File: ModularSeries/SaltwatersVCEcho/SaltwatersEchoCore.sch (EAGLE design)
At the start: 109 parts, among them IC1 PT2399DIL16, Q1 2N3906, Q2 2N3906, Q3 2N3906, Q4 2N3906, Q5 2N3904, Q6 2N3904

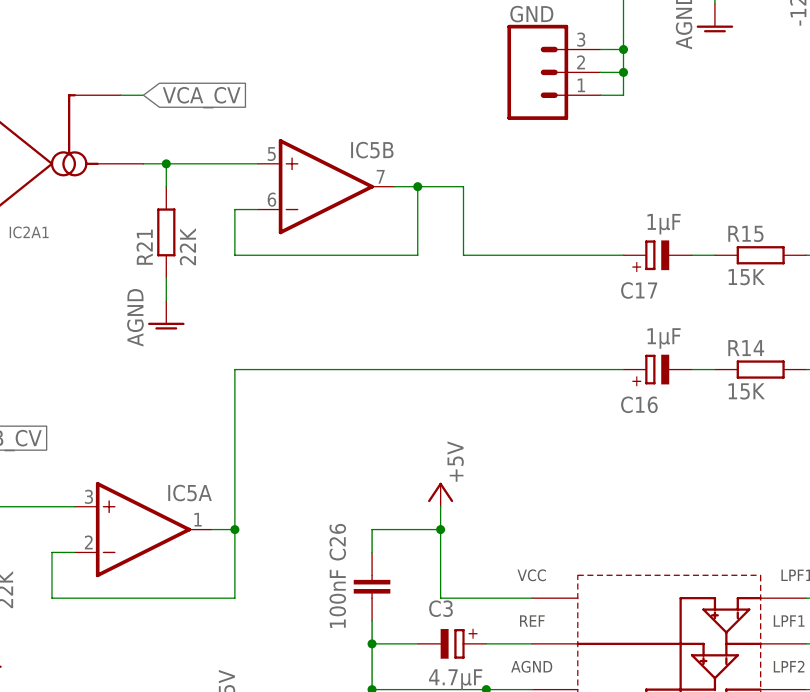
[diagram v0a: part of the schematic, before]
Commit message: All active BOMs updated to new header standard
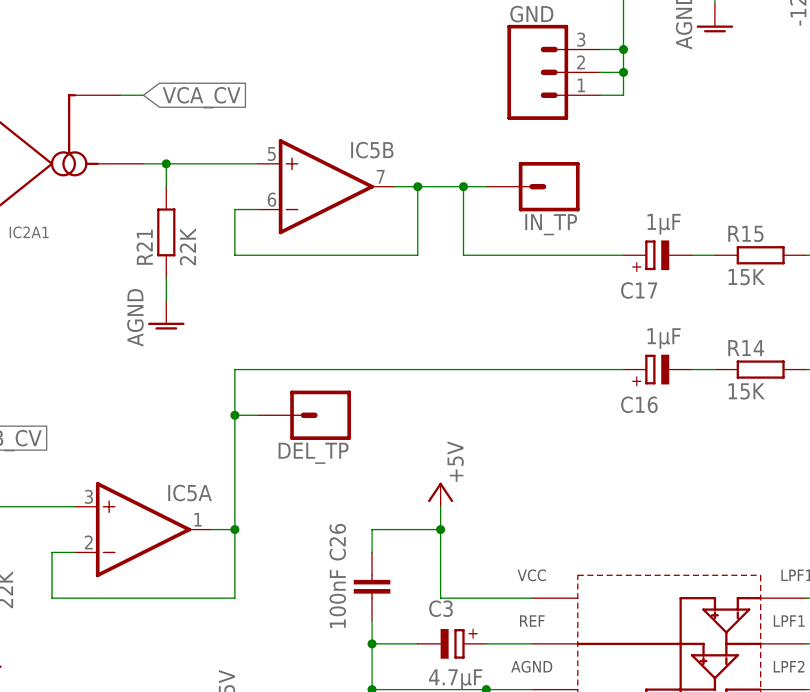
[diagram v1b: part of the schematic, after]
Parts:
- added DEL_TP, IN_TP: 1XWIREPAD, ElectricNoodleBox:1XWIREPAD
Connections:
- net FB_RTN: now also DEL_TP.1
- net N$34: now also IN_TP.1
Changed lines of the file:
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@@
 <part name="AGND21" library="supply1" library_urn="urn:adsk.eagle:library:371" deviceset="AGND" device=""/>
 <part name="GND" library="ElectricNoodleBox" deviceset="3XWIREPAD" device=""/>
+<part name="IN_TP" library="ElectricNoodleBox" deviceset="1XWIREPAD" device=""/>
+<part name="DEL_TP" library="ElectricNoodleBox" deviceset="1XWIREPAD" device=""/>
 </parts>
 <sheets>
@@
 <instance part="GND" gate="G$1" x="55.88" y="127" smashed="yes">
 <attribute name="NAME" x="53.34" y="132.588" size="1.778" layer="95" font="vector"/>
+</instance>
+<instance part="IN_TP" gate="G$1" x="58.42" y="114.3" smashed="yes" rot="R180">
+<attribute name="NAME" x="60.96" y="111.252" size="1.778" layer="95" font="vector" rot="R180"/>
+</instance>
+<instance part="DEL_TP" gate="G$1" x="33.02" y="88.9" smashed="yes" rot="R180">
+<attribute name="NAME" x="35.56" y="85.852" size="1.778" layer="95" font="vector" rot="R180"/>
 </instance>
 </instances>
@@
 <wire x1="22.86" y1="76.2" x2="20.32" y2="76.2" width="0.1524" layer="91"/>
 <junction x="22.86" y="76.2"/>
-<wire x1="22.86" y1="76.2" x2="22.86" y2="93.98" width="0.1524" layer="91"/>
+<wire x1="22.86" y1="76.2" x2="22.86" y2="88.9" width="0.1524" layer="91"/>
+<pinref part="DEL_TP" gate="G$1" pin="1"/>
+<wire x1="22.86" y1="88.9" x2="22.86" y2="93.98" width="0.1524" layer="91"/>
+<wire x1="22.86" y1="88.9" x2="25.4" y2="88.9" width="0.1524" layer="91"/>
+<junction x="22.86" y="88.9"/>
 </segment>
 </net>
@@
 <pinref part="C17" gate="G$1" pin="+"/>
 <wire x1="66.04" y1="106.68" x2="48.26" y2="106.68" width="0.1524" layer="91"/>
-</segment>
-</net>
+<pinref part="IN_TP" gate="G$1" pin="1"/>
+<wire x1="48.26" y1="114.3" x2="50.8" y2="114.3" width="0.1524" layer="91"/>
+<junction x="48.26" y="114.3"/>
+</segment>
+</net>

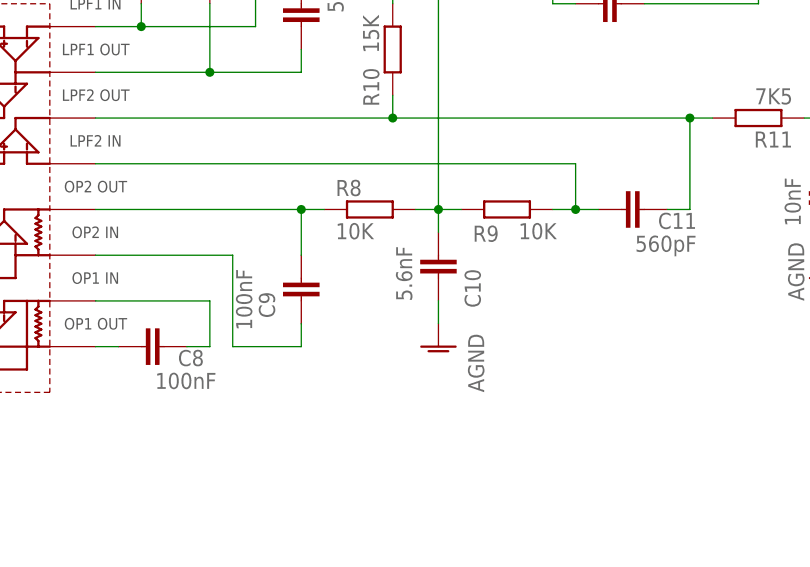
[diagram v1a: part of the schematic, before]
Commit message: Saltwaters BOM added
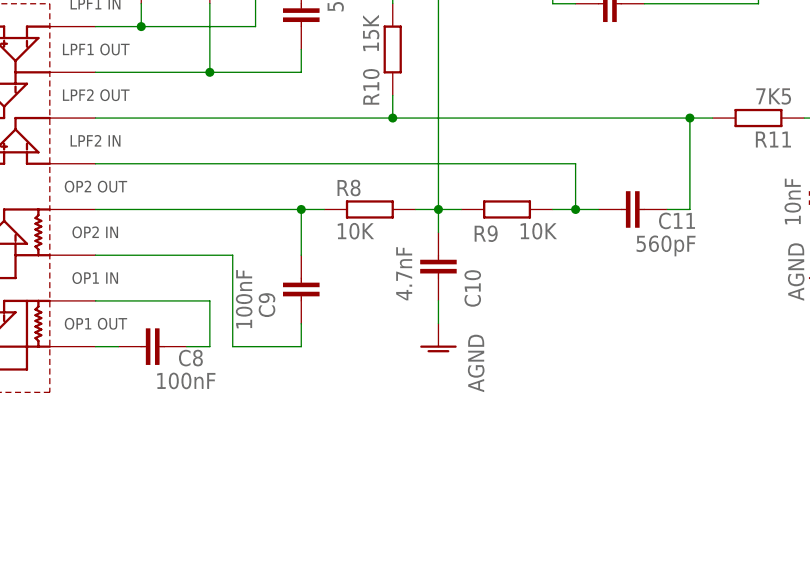
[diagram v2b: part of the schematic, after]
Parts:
- C10: value 5.6nF -> 4.7nF
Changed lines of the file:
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@@
 <part name="C9" library="rcl" library_urn="urn:adsk.eagle:library:334" deviceset="C-EU" device="050-025X075" package3d_urn="urn:adsk.eagle:package:23637/1" value="100nF"/>
 <part name="R8" library="rcl" library_urn="urn:adsk.eagle:library:334" deviceset="R-EU_" device="0207/10" package3d_urn="urn:adsk.eagle:package:23491/2" value="10K"/>
-<part name="C10" library="rcl" library_urn="urn:adsk.eagle:library:334" deviceset="C-EU" device="050-025X075" package3d_urn="urn:adsk.eagle:package:23637/1" value="5.6nF"/>
+<part name="C10" library="rcl" library_urn="urn:adsk.eagle:library:334" deviceset="C-EU" device="050-025X075" package3d_urn="urn:adsk.eagle:package:23637/1" value="4.7nF"/>
 <part name="R9" library="rcl" library_urn="urn:adsk.eagle:library:334" deviceset="R-EU_" device="0207/10" package3d_urn="urn:adsk.eagle:package:23491/2" value="10K"/>
 <part name="AGND6" library="supply1" library_urn="urn:adsk.eagle:library:371" deviceset="AGND" device=""/>
